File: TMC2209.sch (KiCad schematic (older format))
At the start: 30 parts, among them J3 Conn_01x04_Male, U3 TMC2209-LA

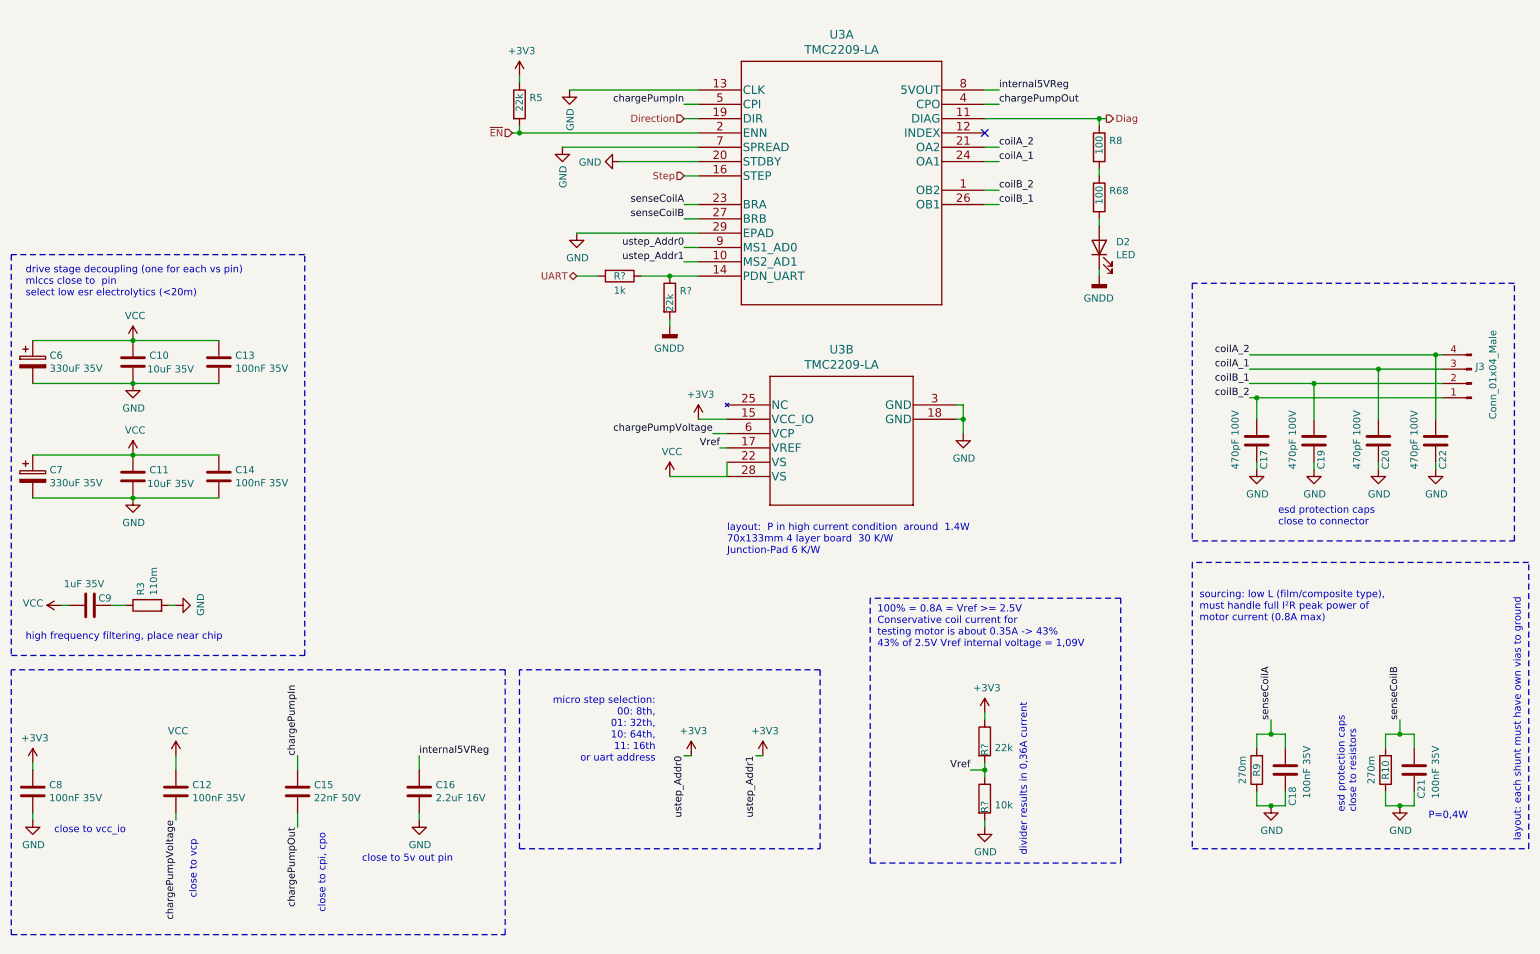
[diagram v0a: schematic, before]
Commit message: Specified dual led resistors Consolidated all grounds to just gnd Consolidated all 3.3 rails to just 3.3V Removed right endstop Removed right wheel angle, servo angle calibration button
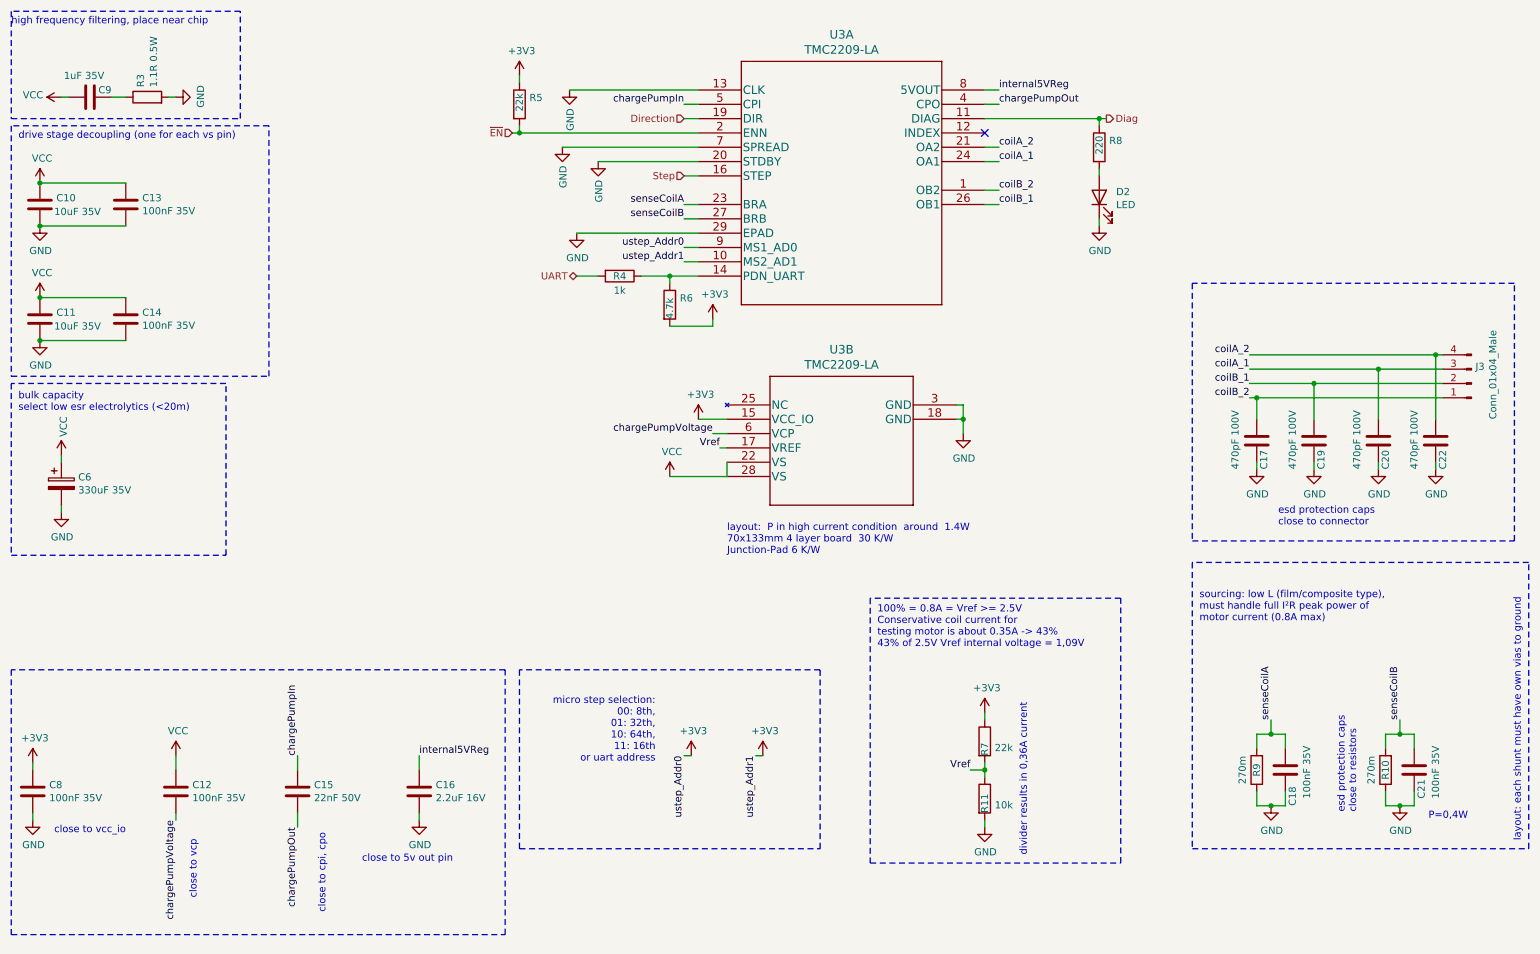
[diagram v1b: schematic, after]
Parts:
- removed C7: 330uF 35V, Capacitor_SMD:CP_Elec_10x10.5, symbol Device:CP
- removed R68: 100, Resistor_SMD:R_0603_1608Metric, symbol Device:R
- R11, R4, R7: renamed from R?; footprint (none) -> Resistor_SMD:R_0603_1608Metric
- R3: value 110m -> 1.1R 0.5W
- R6: renamed from R?; value 22k -> 4.7k
- R8: value 100 -> 220
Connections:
- net +3V3: now also R6.2
- net GND: now also D2.1 (K)
- net at D2.2 (A): now also R8.2
- removed net GNDD: D2.1 (K), R6.2
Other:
- note added: "bulk capacity\nselect low esr electrolytics (<20m)"
- note added: "drive stage decoupling (one for each vs pin)"
- note removed: "drive stage decoupling (one for each vs pin)\nmlccs close to pin\nselect low esr electrolytics (<20m)"
- moved on the sheet: C10, C11, C13, C14, C6, C9, D2, R3, R6

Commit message: wip layout
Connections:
- net coilA_1: now also C19.1, J3.2 (Pin_2); no longer C20.1, J3.3 (Pin_3)
- net coilA_2: now also C17.1, J3.1 (Pin_1); no longer C22.1, J3.4 (Pin_4)
- net coilB_1: now also C20.1, J3.3 (Pin_3); no longer C19.1, J3.2 (Pin_2)
- net coilB_2: now also C22.1, J3.4 (Pin_4); no longer C17.1, J3.1 (Pin_1)
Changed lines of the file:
@@
 	-1   0    0    1
 $EndComp
+Text Label 9200 3100 2    50   ~ 0
+coilA_1
+Text Label 9200 3200 2    50   ~ 0
+coilA_2
 Text Label 9200 3000 2    50   ~ 0
-coilA_1
+coilB_1
 Text Label 9200 2900 2    50   ~ 0
-coilA_2
-Text Label 9200 3100 2    50   ~ 0
-coilB_1
-Text Label 9200 3200 2    50   ~ 0
 coilB_2
 Text Label 7450 1850 0    50   ~ 0

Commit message: wip layout
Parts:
- removed D2: LED, LED_SMD:LED_0603_1608Metric, symbol Device:LED
- removed R8: 220, Resistor_SMD:R_0603_1608Metric, symbol Device:R
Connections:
- net +3V3: no longer U3.10 (MS2_AD1), U3.9 (MS1_AD0)
- net GND: now also U3.10 (MS2_AD1), U3.9 (MS1_AD0)
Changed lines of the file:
@@
 close to cpi, cpo
-$Comp
-L Device:LED D2
-U 1 1 5F755C96
-P 8150 1800
-AR Path="/5F668894/5F755C96" Ref="D2"  Part="1"
-AR Path="/5F6688EA/5F755C96" Ref="D3"  Part="1"
-AR Path="/5F668910/5F755C96" Ref="D4"  Part="1"
-AR Path="/5F668944/5F755C96" Ref="D5"  Part="1"
-AR Path="/5FBA2AFF/5F755C96" Ref="D2"  Part="1"
-F 0 "D2" V 8189 1682 50  0000 R CNN
-F 1 "LED" V 8098 1682 50  0000 R CNN
-F 2 "LED_SMD:LED_0603_1608Metric" H 8150 1800 50  0001 C CNN
-F 3 "~" H 8150 1800 50  0001 C CNN
-	1    8150 1800
-	0    -1   -1   0
-$EndComp
-Wire Wire Line
-	7350 1250 8150 1250
-$Comp
-L Device:R R8
-U 1 1 5F75A8E3
-P 8150 1450
-AR Path="/5F668894/5F75A8E3" Ref="R8"  Part="1"
-AR Path="/5F6688EA/5F75A8E3" Ref="R20"  Part="1"
-AR Path="/5F668910/5F75A8E3" Ref="R32"  Part="1"
-AR Path="/5F668944/5F75A8E3" Ref="R44"  Part="1"
-AR Path="/5FBA2AFF/5F75A8E3" Ref="R8"  Part="1"
-F 0 "R8" H 8220 1496 50  0000 L CNN
-F 1 "220" V 8150 1400 50  0000 L CNN
-F 2 "Resistor_SMD:R_0603_1608Metric" V 8080 1450 50  0001 C CNN
-F 3 "~" H 8150 1450 50  0001 C CNN
-	1    8150 1450
-	1    0    0    -1
-$EndComp
-Wire Wire Line
-	8150 2000 8150 1950
-Wire Wire Line
-	8150 1300 8150 1250
-Wire Wire Line
-	8150 1250 8200 1250
-Connection ~ 8150 1250
-Wire Wire Line
-	5750 5700 5800 5700
-Wire Wire Line
-	5300 5700 5250 5700
 $Comp
 L Device:C C16
@@
 Text Notes 11100 6300 1    50   ~ 0
 layout: each shunt must have own vias to ground
-Wire Wire Line
-	8150 1650 8150 1600
 $Comp
 L tmc2209:TMC2209-LA U3
@@
 F 3 "" H 5350 3350 50  0001 C CNN
 	1    5350 3350
-	1    0    0    -1
-$EndComp
-$Comp
-L power:+3V3 #PWR0124
-U 1 1 5FBAFD94
-P 5300 5700
-F 0 "#PWR0124" H 5300 5550 50  0001 C CNN
-F 1 "+3V3" H 5315 5873 50  0000 C CNN
-F 2 "" H 5300 5700 50  0001 C CNN
-F 3 "" H 5300 5700 50  0001 C CNN
-	1    5300 5700
-	1    0    0    -1
-$EndComp
-$Comp
-L power:+3V3 #PWR0134
-U 1 1 5FBB616C
-P 5800 5700
-F 0 "#PWR0134" H 5800 5550 50  0001 C CNN
-F 1 "+3V3" H 5815 5873 50  0000 C CNN
-F 2 "" H 5800 5700 50  0001 C CNN
-F 3 "" H 5800 5700 50  0001 C CNN
-	1    5800 5700
 	1    0    0    -1
 $EndComp
@@
 Wire Wire Line
 	5450 2700 5450 2650
+Wire Wire Line
+	4650 1550 5350 1550
 $Comp
 L power:GND #PWR?
-U 1 1 609C5EC7
-P 8150 2000
-AR Path="/5F668894/609C5EC7" Ref="#PWR?"  Part="1"
-AR Path="/5F6688EA/609C5EC7" Ref="#PWR?"  Part="1"
-AR Path="/5F668910/609C5EC7" Ref="#PWR?"  Part="1"
-AR Path="/5F668944/609C5EC7" Ref="#PWR?"  Part="1"
-AR Path="/5FBA2AFF/609C5EC7" Ref="#PWR0181"  Part="1"
-F 0 "#PWR0181" H 8150 1750 50  0001 C CNN
-F 1 "GND" H 8155 1827 50  0000 C CNN
-F 2 "" H 8150 2000 50  0001 C CNN
-F 3 "" H 8150 2000 50  0001 C CNN
-	1    8150 2000
-	1    0    0    -1
-$EndComp
-Wire Wire Line
-	4650 1550 5350 1550
+U 1 1 60BC285D
+P 5350 5700
+AR Path="/5F668894/60BC285D" Ref="#PWR?"  Part="1"
+AR Path="/5F6688EA/60BC285D" Ref="#PWR?"  Part="1"
+AR Path="/5F668910/60BC285D" Ref="#PWR?"  Part="1"
+AR Path="/5F668944/60BC285D" Ref="#PWR?"  Part="1"
+AR Path="/5FBA2AFF/60BC285D" Ref="#PWR0124"  Part="1"
+F 0 "#PWR0124" H 5350 5450 50  0001 C CNN
+F 1 "GND" H 5355 5527 50  0000 C CNN
+F 2 "" H 5350 5700 50  0001 C CNN
+F 3 "" H 5350 5700 50  0001 C CNN
+	1    5350 5700
+	1    0    0    -1
+$EndComp
+$Comp
+L power:GND #PWR?
+U 1 1 60BC2D93
+P 5850 5700
+AR Path="/5F668894/60BC2D93" Ref="#PWR?"  Part="1"
+AR Path="/5F6688EA/60BC2D93" Ref="#PWR?"  Part="1"
+AR Path="/5F668910/60BC2D93" Ref="#PWR?"  Part="1"
+AR Path="/5F668944/60BC2D93" Ref="#PWR?"  Part="1"
+AR Path="/5FBA2AFF/60BC2D93" Ref="#PWR0134"  Part="1"
+F 0 "#PWR0134" H 5850 5450 50  0001 C CNN
+F 1 "GND" H 5855 5527 50  0000 C CNN
+F 2 "" H 5850 5700 50  0001 C CNN
+F 3 "" H 5850 5700 50  0001 C CNN
+	1    5850 5700
+	1    0    0    -1
+$EndComp
+Wire Wire Line
+	5750 5700 5850 5700
+Wire Wire Line
+	5250 5700 5350 5700
+Wire Wire Line
+	7350 1250 8200 1250
 $EndSCHEMATC
